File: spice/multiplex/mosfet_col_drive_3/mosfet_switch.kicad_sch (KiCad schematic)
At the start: 13 parts, among them Q1 NPN, Q2 PMOS

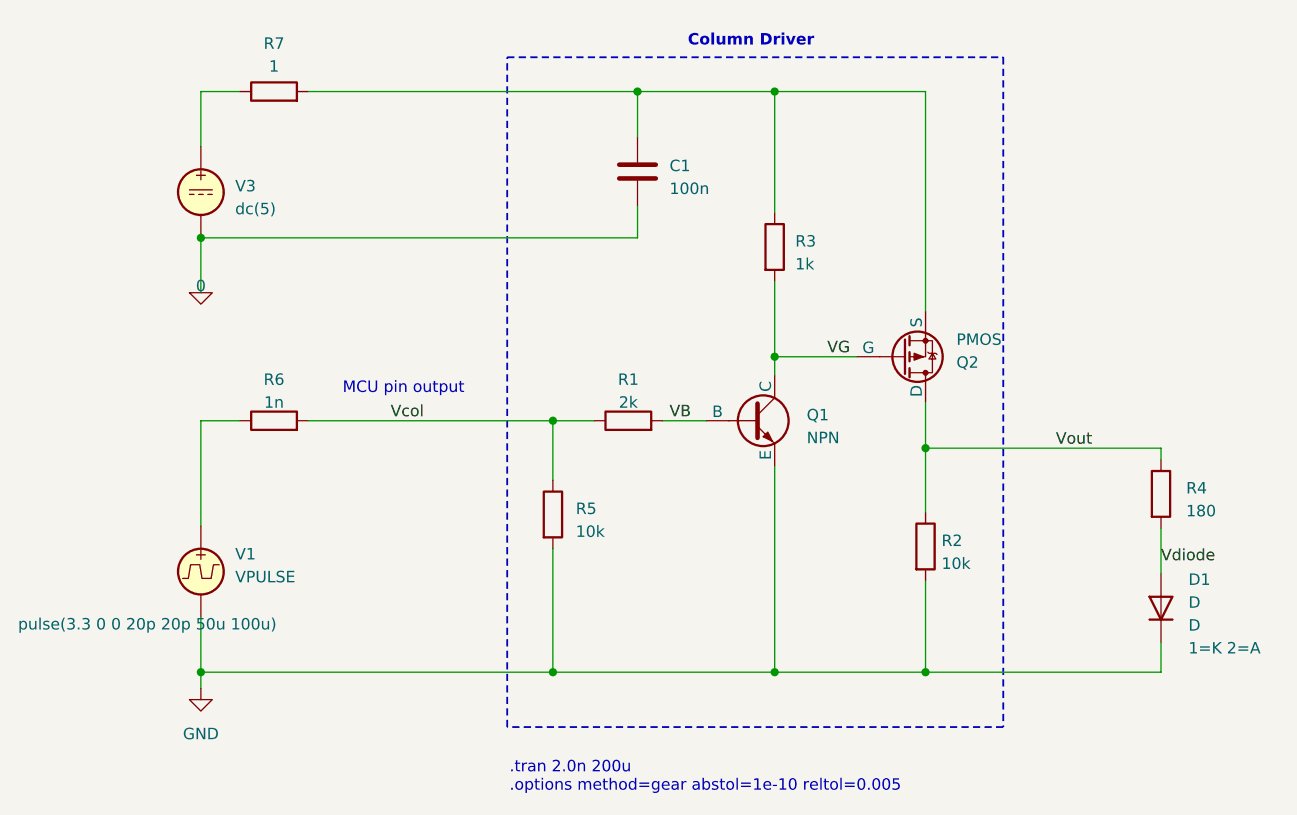
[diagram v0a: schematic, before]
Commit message: Worked on spice models.
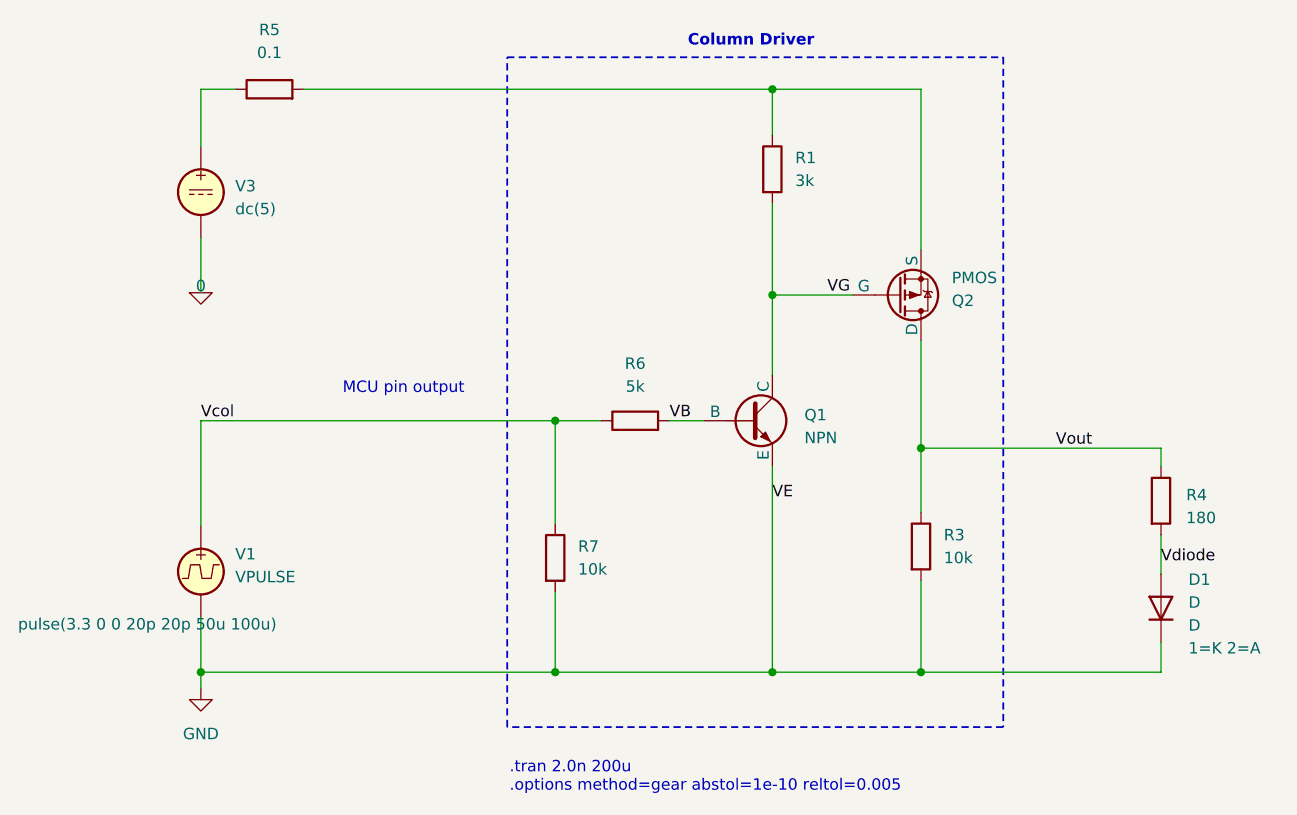
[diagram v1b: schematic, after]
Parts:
- removed C1: 100n, symbol Device:C
- removed R1: 2k, symbol Device:R
- removed R5: 10k, symbol Device:R
- added R7: 10k, symbol Device:R
- R1: renamed from R3; value 1k -> 3k
- R5: renamed from R7; value 1 -> 0.1
- R6: value 1n -> 5k
- renumbered R2 to R3
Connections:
- net GND: now also R7.2
- net VB: now also R6.2
- net Vcol: now also R6.1, V1.1, R7.1; no longer R6.2
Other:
- moved on the sheet: Q2, R1, R3, R4, R5, R6
